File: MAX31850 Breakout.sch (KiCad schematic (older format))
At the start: 11 parts, among them J1 Conn_01x02, J2 Conn_01x03, U1 MAX31850KATB

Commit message: Move library and datasheet folders around
See https://hackaday.com/2017/05/18/kicad-best-practises-library-management/ for more info
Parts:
- U1: symbol MAX31850~Breakout:MAX31850KATB -> MAX31850_Breakout:MAX31850_Breakout_MAX31850KATB
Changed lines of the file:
@@
 $EndDescr
 $Comp
-L MAX31850~Breakout:MAX31850KATB U1
+L MAX31850_Breakout:MAX31850_Breakout_MAX31850KATB U1
 U 1 1 5E73EC25
 P 5300 3300

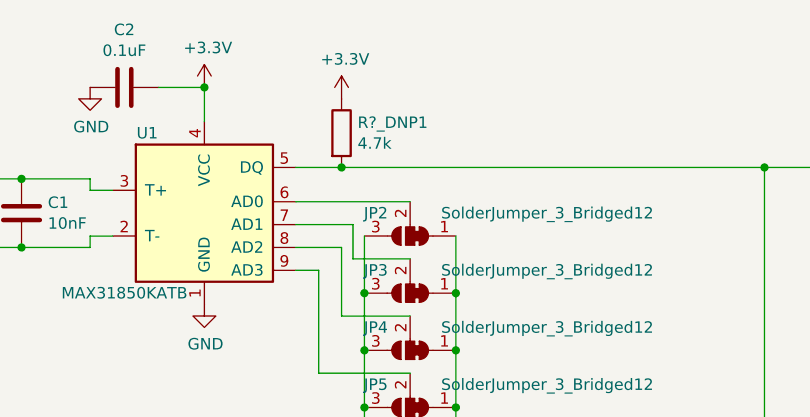
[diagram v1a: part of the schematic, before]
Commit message: Assign footprints
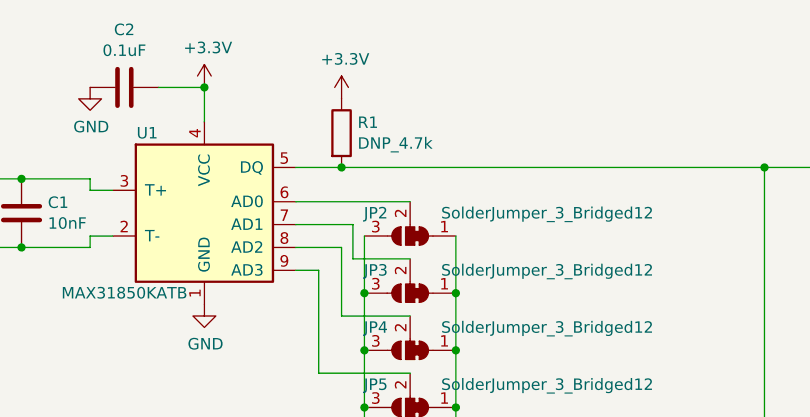
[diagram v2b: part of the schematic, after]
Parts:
- C1, C2: footprint (none) -> 0 - GIE SMD Passive Components:C_0603_1608Metric
- J1: footprint (none) -> 0 - GIE Connectors, Terminal Blocks:TerminalBlock_Phoenix_PT-1,5-2-5.0-H_1x02_P5.00mm_Horizontal
- J2: footprint (none) -> Connector_PinHeader_2.54mm:PinHeader_1x03_P2.54mm_Vertical
- JP1, JP2, JP3, JP4, JP5: footprint (none) -> Jumper:SolderJumper-3_P1.3mm_Bridged12_RoundedPad1.0x1.5mm
- R1: renamed from R?_DNP1; value 4.7k -> DNP_4.7k; footprint (none) -> 0 - GIE SMD Passive Components:R_0603_1608Metric
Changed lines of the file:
@@
 F 0 "JP2" H 6350 3300 50  0000 C CNN
 F 1 "SolderJumper_3_Bridged12" H 5600 3300 50  0000 C CNN
-F 2 "" H 6200 3400 50  0001 C CNN
+F 2 "Jumper:SolderJumper-3_P1.3mm_Bridged12_RoundedPad1.0x1.5mm" H 6200 3400 50  0001 C CNN
 F 3 "~" H 6200 3400 50  0001 C CNN
 	1    6200 3400
@@
 F 0 "JP3" H 6350 3550 50  0000 C CNN
 F 1 "SolderJumper_3_Bridged12" H 5600 3550 50  0000 C CNN
-F 2 "" H 6200 3650 50  0001 C CNN
+F 2 "Jumper:SolderJumper-3_P1.3mm_Bridged12_RoundedPad1.0x1.5mm" H 6200 3650 50  0001 C CNN
 F 3 "~" H 6200 3650 50  0001 C CNN
 	1    6200 3650
@@
 F 0 "JP4" H 6350 3800 50  0000 C CNN
 F 1 "SolderJumper_3_Bridged12" H 5600 3800 50  0000 C CNN
-F 2 "" H 6200 3900 50  0001 C CNN
+F 2 "Jumper:SolderJumper-3_P1.3mm_Bridged12_RoundedPad1.0x1.5mm" H 6200 3900 50  0001 C CNN
 F 3 "~" H 6200 3900 50  0001 C CNN
 	1    6200 3900
@@
 F 0 "JP5" H 6350 4050 50  0000 C CNN
 F 1 "SolderJumper_3_Bridged12" H 5600 4050 50  0000 C CNN
-F 2 "" H 6200 4150 50  0001 C CNN
+F 2 "Jumper:SolderJumper-3_P1.3mm_Bridged12_RoundedPad1.0x1.5mm" H 6200 4150 50  0001 C CNN
 F 3 "~" H 6200 4150 50  0001 C CNN
 	1    6200 4150
@@
 F 0 "JP1" V 6200 4750 50  0000 C CNN
 F 1 "SolderJumper_3_Bridged12" V 6100 5200 50  0000 C CNN
-F 2 "" H 6150 4650 50  0001 C CNN
+F 2 "Jumper:SolderJumper-3_P1.3mm_Bridged12_RoundedPad1.0x1.5mm" H 6150 4650 50  0001 C CNN
 F 3 "~" H 6150 4650 50  0001 C CNN
 	1    6150 4650
@@
 $EndComp
 $Comp
-L Device:R R?_DNP1
-U 1 1 5E7522C3
-P 5900 2950
-F 0 "R?_DNP1" H 5970 2996 50  0000 L CNN
-F 1 "4.7k" H 5970 2905 50  0000 L CNN
-F 2 "" V 5830 2950 50  0001 C CNN
-F 3 "~" H 5900 2950 50  0001 C CNN
-	1    5900 2950
-	1    0    0    -1
-$EndComp
-$Comp
 L Device:C C2
 U 1 1 5E752F56
@@
 F 0 "C2" V 4698 2750 50  0000 C CNN
 F 1 "0.1uF" V 4789 2750 50  0000 C CNN
-F 2 "" H 4988 2600 50  0001 C CNN
+F 2 "0 - GIE SMD Passive Components:C_0603_1608Metric" H 4988 2600 50  0001 C CNN
 F 3 "~" H 4950 2750 50  0001 C CNN
 	1    4950 2750
@@
 F 0 "J2" H 8730 3042 50  0000 L CNN
 F 1 "Conn_01x03" H 8730 2951 50  0000 L CNN
-F 2 "" H 8650 3000 50  0001 C CNN
+F 2 "Connector_PinHeader_2.54mm:PinHeader_1x03_P2.54mm_Vertical" H 8650 3000 50  0001 C CNN
 F 3 "~" H 8650 3000 50  0001 C CNN
 	1    8650 3000
@@
 F 0 "C1" H 4615 3346 50  0000 L CNN
 F 1 "10nF" H 4615 3255 50  0000 L CNN
-F 2 "" H 4538 3150 50  0001 C CNN
+F 2 "0 - GIE SMD Passive Components:C_0603_1608Metric" H 4538 3150 50  0001 C CNN
 F 3 "~" H 4500 3300 50  0001 C CNN
 	1    4500 3300
@@
 F 0 "J1" H 3868 3025 50  0000 C CNN
 F 1 "Conn_01x02" H 3868 3116 50  0000 C CNN
-F 2 "" H 3950 3350 50  0001 C CNN
+F 2 "0 - GIE Connectors, Terminal Blocks:TerminalBlock_Phoenix_PT-1,5-2-5.0-H_1x02_P5.00mm_Horizontal" H 3950 3350 50  0001 C CNN
 F 3 "~" H 3950 3350 50  0001 C CNN
 	1    3950 3350
@@
 Wire Wire Line
 	7750 3100 8450 3100
+$Comp
+L Device:R R1
+U 1 1 5E7522C3
+P 5900 2950
+F 0 "R1" H 5970 2996 50  0000 L CNN
+F 1 "DNP_4.7k" H 5970 2905 50  0000 L CNN
+F 2 "0 - GIE SMD Passive Components:R_0603_1608Metric" V 5830 2950 50  0001 C CNN
+F 3 "~" H 5900 2950 50  0001 C CNN
+	1    5900 2950
+	1    0    0    -1
+$EndComp
 $EndSCHEMATC

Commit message: Update Jumper component, label all nets
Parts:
- JP1, JP2, JP3, JP4, JP5: symbol Jumper:SolderJumper_3_Bridged12 -> 0-GIE_SMD_Jumpers:SolderJumper_3_Bridged12
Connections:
- net T-: now reaches C1.2, J1.1 (Pin_1), U1.2 (T-)
- net T+: now reaches C1.1, J1.2 (Pin_2), U1.3 (T+)
- net DQ: now reaches J2.3 (Pin_3), JP1.3 (B), R1.2, U1.5 (DQ)
- net AD0: now reaches JP2.2 (C), U1.6 (AD0)
- net AD1: now reaches JP3.2 (C), U1.7 (AD1)
- net AD2: now reaches JP4.2 (C), U1.8 (AD2)
- net AD3: now reaches JP5.2 (C), U1.9 (AD3)
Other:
- moved on the sheet: JP1, JP3, JP4, JP5
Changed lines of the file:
@@
 	1    0    0    -1
 $EndComp
-$Comp
-L Jumper:SolderJumper_3_Bridged12 JP2
-U 1 1 5E7420FC
-P 6200 3400
-F 0 "JP2" H 6350 3300 50  0000 C CNN
-F 1 "SolderJumper_3_Bridged12" H 5600 3300 50  0000 C CNN
-F 2 "Jumper:SolderJumper-3_P1.3mm_Bridged12_RoundedPad1.0x1.5mm" H 6200 3400 50  0001 C CNN
-F 3 "~" H 6200 3400 50  0001 C CNN
-	1    6200 3400
-	-1   0    0    1
-$EndComp
-$Comp
-L Jumper:SolderJumper_3_Bridged12 JP3
-U 1 1 5E746EFF
-P 6200 3650
-F 0 "JP3" H 6350 3550 50  0000 C CNN
-F 1 "SolderJumper_3_Bridged12" H 5600 3550 50  0000 C CNN
-F 2 "Jumper:SolderJumper-3_P1.3mm_Bridged12_RoundedPad1.0x1.5mm" H 6200 3650 50  0001 C CNN
-F 3 "~" H 6200 3650 50  0001 C CNN
-	1    6200 3650
-	-1   0    0    1
-$EndComp
-$Comp
-L Jumper:SolderJumper_3_Bridged12 JP4
-U 1 1 5E747464
-P 6200 3900
-F 0 "JP4" H 6350 3800 50  0000 C CNN
-F 1 "SolderJumper_3_Bridged12" H 5600 3800 50  0000 C CNN
-F 2 "Jumper:SolderJumper-3_P1.3mm_Bridged12_RoundedPad1.0x1.5mm" H 6200 3900 50  0001 C CNN
-F 3 "~" H 6200 3900 50  0001 C CNN
-	1    6200 3900
-	-1   0    0    1
-$EndComp
-$Comp
-L Jumper:SolderJumper_3_Bridged12 JP5
-U 1 1 5E7479F9
-P 6200 4150
-F 0 "JP5" H 6350 4050 50  0000 C CNN
-F 1 "SolderJumper_3_Bridged12" H 5600 4050 50  0000 C CNN
-F 2 "Jumper:SolderJumper-3_P1.3mm_Bridged12_RoundedPad1.0x1.5mm" H 6200 4150 50  0001 C CNN
-F 3 "~" H 6200 4150 50  0001 C CNN
-	1    6200 4150
-	-1   0    0    1
-$EndComp
-$Comp
-L power:GND #PWR06
-U 1 1 5E74B9A8
-P 6400 4200
-F 0 "#PWR06" H 6400 3950 50  0001 C CNN
-F 1 "GND" H 6405 4027 50  0000 C CNN
-F 2 "" H 6400 4200 50  0001 C CNN
-F 3 "" H 6400 4200 50  0001 C CNN
-	1    6400 4200
-	1    0    0    -1
-$EndComp
-$Comp
-L Jumper:SolderJumper_3_Bridged12 JP1
-U 1 1 5E74BD6C
-P 6150 4650
-F 0 "JP1" V 6200 4750 50  0000 C CNN
-F 1 "SolderJumper_3_Bridged12" V 6100 5200 50  0000 C CNN
-F 2 "Jumper:SolderJumper-3_P1.3mm_Bridged12_RoundedPad1.0x1.5mm" H 6150 4650 50  0001 C CNN
-F 3 "~" H 6150 4650 50  0001 C CNN
-	1    6150 4650
-	0    1    1    0
-$EndComp
-Wire Wire Line
-	6000 4650 6000 4150
-Connection ~ 6000 3650
-Wire Wire Line
-	6000 3650 6000 3400
-Connection ~ 6000 3900
-Wire Wire Line
-	6000 3900 6000 3650
-Connection ~ 6000 4150
-Wire Wire Line
-	6000 4150 6000 3900
-Wire Wire Line
-	6400 3400 6400 3650
-Connection ~ 6400 3650
-Wire Wire Line
-	6400 3650 6400 3900
-Connection ~ 6400 3900
-Wire Wire Line
-	6400 3900 6400 4150
-Connection ~ 6400 4150
-Wire Wire Line
-	6400 4150 6400 4200
 Wire Wire Line
 	6200 3250 5700 3250
-Wire Wire Line
-	6200 3500 5950 3500
-Wire Wire Line
-	5950 3500 5950 3350
-Wire Wire Line
-	5950 3350 5700 3350
-Wire Wire Line
-	5700 3450 5900 3450
-Wire Wire Line
-	5900 3450 5900 3750
-Wire Wire Line
-	5900 3750 6200 3750
-Wire Wire Line
-	6200 4000 5800 4000
-Wire Wire Line
-	5800 4000 5800 3550
-Wire Wire Line
-	5800 3550 5700 3550
-$Comp
-L power:+3.3V #PWR05
-U 1 1 5E7518A6
-P 6150 4450
-F 0 "#PWR05" H 6150 4300 50  0001 C CNN
-F 1 "+3.3V" H 6165 4623 50  0000 C CNN
-F 2 "" H 6150 4450 50  0001 C CNN
-F 3 "" H 6150 4450 50  0001 C CNN
-	1    6150 4450
-	1    0    0    -1
-$EndComp
 $Comp
 L Device:C C2
@@
 	1    0    0    -1
 $EndComp
-Wire Wire Line
-	5900 3100 7750 3100
-Connection ~ 5900 3100
 $Comp
 L power:+3.3V #PWR04
@@
 L power:GND #PWR07
 U 1 1 5E757CA6
-P 8250 2850
-F 0 "#PWR07" H 8250 2600 50  0001 C CNN
-F 1 "GND" H 8255 2677 50  0000 C CNN
-F 2 "" H 8250 2850 50  0001 C CNN
-F 3 "" H 8250 2850 50  0001 C CNN
-	1    8250 2850
+P 8200 3000
+F 0 "#PWR07" H 8200 2750 50  0001 C CNN
+F 1 "GND" H 8205 2827 50  0000 C CNN
+F 2 "" H 8200 3000 50  0001 C CNN
+F 3 "" H 8200 3000 50  0001 C CNN
+	1    8200 3000
 	1    0    0    -1
 $EndComp
@@
 L power:+3.3V #PWR08
 U 1 1 5E7589FC
-P 8450 2900
-F 0 "#PWR08" H 8450 2750 50  0001 C CNN
-F 1 "+3.3V" H 8465 3073 50  0000 C CNN
-F 2 "" H 8450 2900 50  0001 C CNN
-F 3 "" H 8450 2900 50  0001 C CNN
-	1    8450 2900
-	1    0    0    -1
-$EndComp
-Wire Wire Line
-	8250 2850 8350 2850
-Wire Wire Line
-	8350 2850 8350 3000
-Wire Wire Line
-	8350 3000 8450 3000
+P 8200 2900
+F 0 "#PWR08" H 8200 2750 50  0001 C CNN
+F 1 "+3.3V" H 8215 3073 50  0000 C CNN
+F 2 "" H 8200 2900 50  0001 C CNN
+F 3 "" H 8200 2900 50  0001 C CNN
+	1    8200 2900
+	1    0    0    -1
+$EndComp
 $Comp
 L Device:C C1
@@
 Wire Wire Line
 	4300 3150 4500 3150
-Wire Wire Line
-	7750 3100 7750 4850
-Wire Wire Line
-	7750 4850 6150 4850
-Connection ~ 7750 3100
-Wire Wire Line
-	7750 3100 8450 3100
 $Comp
 L Device:R R1
@@
 	1    0    0    -1
 $EndComp
+$Comp
+L power:PWR_FLAG #FLG0101
+U 1 1 5E76A609
+P 8200 2900
+F 0 "#FLG0101" H 8200 2975 50  0001 C CNN
+F 1 "PWR_FLAG" V 8200 3027 50  0000 L CNN
+F 2 "" H 8200 2900 50  0001 C CNN
+F 3 "~" H 8200 2900 50  0001 C CNN
+	1    8200 2900
+	0    -1   -1   0
+$EndComp
+Text Label 8450 3100 2    50   ~ 0
+DQ
+Text Label 5700 3100 0    50   ~ 0
+DQ
+Text Label 6150 5000 3    50   ~ 0
+DQ
+Wire Wire Line
+	8200 3000 8450 3000
+Connection ~ 8200 2900
+Wire Wire Line
+	8200 2900 8450 2900
+$Comp
+L power:PWR_FLAG #FLG0102
+U 1 1 5E771B67
+P 8200 3000
+F 0 "#FLG0102" H 8200 3075 50  0001 C CNN
+F 1 "PWR_FLAG" V 8200 3127 50  0000 L CNN
+F 2 "" H 8200 3000 50  0001 C CNN
+F 3 "~" H 8200 3000 50  0001 C CNN
+	1    8200 3000
+	0    -1   -1   0
+$EndComp
+Connection ~ 8200 3000
+Text Label 5700 3250 0    50   ~ 0
+AD0
+Text Label 5700 3350 0    50   ~ 0
+AD1
+Text Label 5700 3450 0    50   ~ 0
+AD2
+Text Label 5700 3550 0    50   ~ 0
+AD3
+$Comp
+L power:+3.3V #PWR05
+U 1 1 5E7518A6
+P 6150 4600
+F 0 "#PWR05" H 6150 4450 50  0001 C CNN
+F 1 "+3.3V" H 6165 4773 50  0000 C CNN
+F 2 "" H 6150 4600 50  0001 C CNN
+F 3 "" H 6150 4600 50  0001 C CNN
+	1    6150 4600
+	1    0    0    -1
+$EndComp
+Wire Wire Line
+	6400 4300 6400 4350
+Wire Wire Line
+	6000 4800 6000 4300
+$Comp
+L power:GND #PWR06
+U 1 1 5E74B9A8
+P 6400 4350
+F 0 "#PWR06" H 6400 4100 50  0001 C CNN
+F 1 "GND" H 6405 4177 50  0000 C CNN
+F 2 "" H 6400 4350 50  0001 C CNN
+F 3 "" H 6400 4350 50  0001 C CNN
+	1    6400 4350
+	1    0    0    -1
+$EndComp
+$Comp
+L 0-GIE_SMD_Jumpers:SolderJumper_3_Bridged12 JP5
+U 1 1 5E7479F9
+P 6200 4300
+F 0 "JP5" H 6350 4200 50  0000 C CNN
+F 1 "SolderJumper_3_Bridged12" H 5600 4200 50  0000 C CNN
+F 2 "Jumper:SolderJumper-3_P1.3mm_Bridged12_RoundedPad1.0x1.5mm" H 6200 4300 50  0001 C CNN
+F 3 "~" H 6200 4300 50  0001 C CNN
+	1    6200 4300
+	-1   0    0    1
+$EndComp
+$Comp
+L 0-GIE_SMD_Jumpers:SolderJumper_3_Bridged12 JP4
+U 1 1 5E747464
+P 6200 4000
+F 0 "JP4" H 6350 3900 50  0000 C CNN
+F 1 "SolderJumper_3_Bridged12" H 5600 3900 50  0000 C CNN
+F 2 "Jumper:SolderJumper-3_P1.3mm_Bridged12_RoundedPad1.0x1.5mm" H 6200 4000 50  0001 C CNN
+F 3 "~" H 6200 4000 50  0001 C CNN
+	1    6200 4000
+	-1   0    0    1
+$EndComp
+$Comp
+L 0-GIE_SMD_Jumpers:SolderJumper_3_Bridged12 JP3
+U 1 1 5E746EFF
+P 6200 3700
+F 0 "JP3" H 6350 3600 50  0000 C CNN
+F 1 "SolderJumper_3_Bridged12" H 5600 3600 50  0000 C CNN
+F 2 "Jumper:SolderJumper-3_P1.3mm_Bridged12_RoundedPad1.0x1.5mm" H 6200 3700 50  0001 C CNN
+F 3 "~" H 6200 3700 50  0001 C CNN
+	1    6200 3700
+	-1   0    0    1
+$EndComp
+$Comp
+L 0-GIE_SMD_Jumpers:SolderJumper_3_Bridged12 JP2
+U 1 1 5E7420FC
+P 6200 3400
+F 0 "JP2" H 6350 3300 50  0000 C CNN
+F 1 "SolderJumper_3_Bridged12" H 5600 3300 50  0000 C CNN
+F 2 "Jumper:SolderJumper-3_P1.3mm_Bridged12_RoundedPad1.0x1.5mm" H 6200 3400 50  0001 C CNN
+F 3 "~" H 6200 3400 50  0001 C CNN
+	1    6200 3400
+	-1   0    0    1
+$EndComp
+Text Label 6200 3550 0    50   ~ 0
+AD1
+Text Label 6200 3850 0    50   ~ 0
+AD2
+Text Label 6200 4150 0    50   ~ 0
+AD3
+Wire Wire Line
+	6000 3400 6000 3700
+Connection ~ 6000 4300
+Connection ~ 6000 3700
+Wire Wire Line
+	6000 3700 6000 4000
+Connection ~ 6000 4000
+Wire Wire Line
+	6000 4000 6000 4300
+Wire Wire Line
+	6400 3400 6400 3700
+Connection ~ 6400 4300
+Connection ~ 6400 3700
+Wire Wire Line
+	6400 3700 6400 4000
+Connection ~ 6400 4000
+Wire Wire Line
+	6400 4000 6400 4300
+$Comp
+L 0-GIE_SMD_Jumpers:SolderJumper_3_Bridged12 JP1
+U 1 1 5E74BD6C
+P 6150 4800
+F 0 "JP1" V 6200 4900 50  0000 C CNN
+F 1 "SolderJumper_3_Bridged12" V 6100 5350 50  0000 C CNN
+F 2 "Jumper:SolderJumper-3_P1.3mm_Bridged12_RoundedPad1.0x1.5mm" H 6150 4800 50  0001 C CNN
+F 3 "~" H 6150 4800 50  0001 C CNN
+	1    6150 4800
+	0    1    1    0
+$EndComp
+Text Label 4700 3150 0    50   ~ 0
+T+
+Text Label 4700 3450 0    50   ~ 0
+T-
 $EndSCHEMATC

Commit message: Update project library
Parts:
- U1: symbol MAX31850_Breakout:MAX31850_Breakout_MAX31850KATB -> MAX31850_Breakout:MAX31850KATB
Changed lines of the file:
@@
 $EndDescr
 $Comp
-L MAX31850_Breakout:MAX31850_Breakout_MAX31850KATB U1
+L MAX31850_Breakout:MAX31850KATB U1
 U 1 1 5E73EC25
 P 5300 3300

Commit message: Layout and Route PCB
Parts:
- renumbered JP2 to AD0, JP3 to AD1, JP4 to AD2, JP5 to AD3, JP1 to AD_SRC1
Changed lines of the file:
@@
 $EndComp
 $Comp
-L 0-GIE_SMD_Jumpers:SolderJumper_3_Bridged12 JP5
+L 0-GIE_SMD_Jumpers:SolderJumper_3_Bridged12 AD3
 U 1 1 5E7479F9
 P 6200 4300
-F 0 "JP5" H 6350 4200 50  0000 C CNN
+F 0 "AD3" H 6350 4200 50  0000 C CNN
 F 1 "SolderJumper_3_Bridged12" H 5600 4200 50  0000 C CNN
 F 2 "Jumper:SolderJumper-3_P1.3mm_Bridged12_RoundedPad1.0x1.5mm" H 6200 4300 50  0001 C CNN
@@
 $EndComp
 $Comp
-L 0-GIE_SMD_Jumpers:SolderJumper_3_Bridged12 JP4
+L 0-GIE_SMD_Jumpers:SolderJumper_3_Bridged12 AD2
 U 1 1 5E747464
 P 6200 4000
-F 0 "JP4" H 6350 3900 50  0000 C CNN
+F 0 "AD2" H 6350 3900 50  0000 C CNN
 F 1 "SolderJumper_3_Bridged12" H 5600 3900 50  0000 C CNN
 F 2 "Jumper:SolderJumper-3_P1.3mm_Bridged12_RoundedPad1.0x1.5mm" H 6200 4000 50  0001 C CNN
@@
 $EndComp
 $Comp
-L 0-GIE_SMD_Jumpers:SolderJumper_3_Bridged12 JP3
+L 0-GIE_SMD_Jumpers:SolderJumper_3_Bridged12 AD1
 U 1 1 5E746EFF
 P 6200 3700
-F 0 "JP3" H 6350 3600 50  0000 C CNN
+F 0 "AD1" H 6350 3600 50  0000 C CNN
 F 1 "SolderJumper_3_Bridged12" H 5600 3600 50  0000 C CNN
 F 2 "Jumper:SolderJumper-3_P1.3mm_Bridged12_RoundedPad1.0x1.5mm" H 6200 3700 50  0001 C CNN
@@
 $EndComp
 $Comp
-L 0-GIE_SMD_Jumpers:SolderJumper_3_Bridged12 JP2
+L 0-GIE_SMD_Jumpers:SolderJumper_3_Bridged12 AD0
 U 1 1 5E7420FC
 P 6200 3400
-F 0 "JP2" H 6350 3300 50  0000 C CNN
+F 0 "AD0" H 6350 3300 50  0000 C CNN
 F 1 "SolderJumper_3_Bridged12" H 5600 3300 50  0000 C CNN
 F 2 "Jumper:SolderJumper-3_P1.3mm_Bridged12_RoundedPad1.0x1.5mm" H 6200 3400 50  0001 C CNN
@@
 	6400 4000 6400 4300
 $Comp
-L 0-GIE_SMD_Jumpers:SolderJumper_3_Bridged12 JP1
+L 0-GIE_SMD_Jumpers:SolderJumper_3_Bridged12 AD_SRC1
 U 1 1 5E74BD6C
 P 6150 4800
-F 0 "JP1" V 6200 4900 50  0000 C CNN
+F 0 "AD_SRC1" V 6200 5000 50  0000 C CNN
 F 1 "SolderJumper_3_Bridged12" V 6100 5350 50  0000 C CNN
 F 2 "Jumper:SolderJumper-3_P1.3mm_Bridged12_RoundedPad1.0x1.5mm" H 6150 4800 50  0001 C CNN

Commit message: Replace footprints with local copy
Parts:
- AD0, AD1, AD2, AD3, AD_SRC1: footprint Jumper:SolderJumper-3_P1.3mm_Bridged12_RoundedPad1.0x1.5mm -> MAX31850-Breakout-footprints:SolderJumper-3_P1.3mm_Bridged12_RoundedPad1.0x1.5mm
- C1, C2: footprint 0 - GIE SMD Passive Components:C_0603_1608Metric -> MAX31850-Breakout-footprints:C_0603_1608Metric
- J1: footprint 0 - GIE Connectors, Terminal Blocks:TerminalBlock_Phoenix_PT-1,5-2-5.0-H_1x02_P5.00mm_Horizontal -> MAX31850-Breakout-footprints:TerminalBlock_Phoenix_PT-1,5-2-5.0-H_1x02_P5.00mm_Horizontal
- J2: footprint Connector_PinHeader_2.54mm:PinHeader_1x03_P2.54mm_Vertical -> MAX31850-Breakout-footprints:PinHeader_1x03_P2.54mm_Vertical
- R1: footprint 0 - GIE SMD Passive Components:R_0603_1608Metric -> MAX31850-Breakout-footprints:R_0603_1608Metric
- U1: footprint MAX31850-Breakout:TDFN-10-1EP_3x4mm_P0.5mm_EP1.75x2.7mm -> MAX31850-Breakout-footprints:TDFN-10-1EP_3x4mm_P0.5mm_EP1.75x2.7mm
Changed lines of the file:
@@
 EESchema Schematic File Version 4
+LIBS:MAX31850 Breakout-cache
 EELAYER 30 0
 EELAYER END
@@
 F 0 "U1" H 5050 3650 50  0000 C CNN
 F 1 "MAX31850KATB" H 4950 2950 50  0000 C CNN
-F 2 "MAX31850-Breakout:TDFN-10-1EP_3x4mm_P0.5mm_EP1.75x2.7mm" H 6300 2950 50  0001 C CIN
+F 2 "MAX31850-Breakout-footprints:TDFN-10-1EP_3x4mm_P0.5mm_EP1.75x2.7mm" H 6300 2950 50  0001 C CIN
 F 3 "https://datasheets.maximintegrated.com/en/ds/MAX31850-MAX31851.pdf" H 5300 3300 50  0001 C CNN
 	1    5300 3300
@@
 F 0 "C2" V 4698 2750 50  0000 C CNN
 F 1 "0.1uF" V 4789 2750 50  0000 C CNN
-F 2 "0 - GIE SMD Passive Components:C_0603_1608Metric" H 4988 2600 50  0001 C CNN
+F 2 "MAX31850-Breakout-footprints:C_0603_1608Metric" H 4988 2600 50  0001 C CNN
 F 3 "~" H 4950 2750 50  0001 C CNN
 	1    4950 2750
@@
 F 0 "J2" H 8730 3042 50  0000 L CNN
 F 1 "Conn_01x03" H 8730 2951 50  0000 L CNN
-F 2 "Connector_PinHeader_2.54mm:PinHeader_1x03_P2.54mm_Vertical" H 8650 3000 50  0001 C CNN
+F 2 "MAX31850-Breakout-footprints:PinHeader_1x03_P2.54mm_Vertical" H 8650 3000 50  0001 C CNN
 F 3 "~" H 8650 3000 50  0001 C CNN
 	1    8650 3000
@@
 F 0 "C1" H 4615 3346 50  0000 L CNN
 F 1 "10nF" H 4615 3255 50  0000 L CNN
-F 2 "0 - GIE SMD Passive Components:C_0603_1608Metric" H 4538 3150 50  0001 C CNN
+F 2 "MAX31850-Breakout-footprints:C_0603_1608Metric" H 4538 3150 50  0001 C CNN
 F 3 "~" H 4500 3300 50  0001 C CNN
 	1    4500 3300
@@
 F 0 "J1" H 3868 3025 50  0000 C CNN
 F 1 "Conn_01x02" H 3868 3116 50  0000 C CNN
-F 2 "0 - GIE Connectors, Terminal Blocks:TerminalBlock_Phoenix_PT-1,5-2-5.0-H_1x02_P5.00mm_Horizontal" H 3950 3350 50  0001 C CNN
+F 2 "MAX31850-Breakout-footprints:TerminalBlock_Phoenix_PT-1,5-2-5.0-H_1x02_P5.00mm_Horizontal" H 3950 3350 50  0001 C CNN
 F 3 "~" H 3950 3350 50  0001 C CNN
 	1    3950 3350
@@
 F 0 "R1" H 5970 2996 50  0000 L CNN
 F 1 "DNP_4.7k" H 5970 2905 50  0000 L CNN
-F 2 "0 - GIE SMD Passive Components:R_0603_1608Metric" V 5830 2950 50  0001 C CNN
+F 2 "MAX31850-Breakout-footprints:R_0603_1608Metric" V 5830 2950 50  0001 C CNN
 F 3 "~" H 5900 2950 50  0001 C CNN
 	1    5900 2950
@@
 F 0 "AD3" H 6350 4200 50  0000 C CNN
 F 1 "SolderJumper_3_Bridged12" H 5600 4200 50  0000 C CNN
-F 2 "Jumper:SolderJumper-3_P1.3mm_Bridged12_RoundedPad1.0x1.5mm" H 6200 4300 50  0001 C CNN
+F 2 "MAX31850-Breakout-footprints:SolderJumper-3_P1.3mm_Bridged12_RoundedPad1.0x1.5mm" H 6200 4300 50  0001 C CNN
 F 3 "~" H 6200 4300 50  0001 C CNN
 	1    6200 4300
@@
 F 0 "AD2" H 6350 3900 50  0000 C CNN
 F 1 "SolderJumper_3_Bridged12" H 5600 3900 50  0000 C CNN
-F 2 "Jumper:SolderJumper-3_P1.3mm_Bridged12_RoundedPad1.0x1.5mm" H 6200 4000 50  0001 C CNN
+F 2 "MAX31850-Breakout-footprints:SolderJumper-3_P1.3mm_Bridged12_RoundedPad1.0x1.5mm" H 6200 4000 50  0001 C CNN
 F 3 "~" H 6200 4000 50  0001 C CNN
 	1    6200 4000
@@
 F 0 "AD1" H 6350 3600 50  0000 C CNN
 F 1 "SolderJumper_3_Bridged12" H 5600 3600 50  0000 C CNN
-F 2 "Jumper:SolderJumper-3_P1.3mm_Bridged12_RoundedPad1.0x1.5mm" H 6200 3700 50  0001 C CNN
+F 2 "MAX31850-Breakout-footprints:SolderJumper-3_P1.3mm_Bridged12_RoundedPad1.0x1.5mm" H 6200 3700 50  0001 C CNN
 F 3 "~" H 6200 3700 50  0001 C CNN
 	1    6200 3700
@@
 F 0 "AD0" H 6350 3300 50  0000 C CNN
 F 1 "SolderJumper_3_Bridged12" H 5600 3300 50  0000 C CNN
-F 2 "Jumper:SolderJumper-3_P1.3mm_Bridged12_RoundedPad1.0x1.5mm" H 6200 3400 50  0001 C CNN
+F 2 "MAX31850-Breakout-footprints:SolderJumper-3_P1.3mm_Bridged12_RoundedPad1.0x1.5mm" H 6200 3400 50  0001 C CNN
 F 3 "~" H 6200 3400 50  0001 C CNN
 	1    6200 3400
@@
 F 0 "AD_SRC1" V 6200 5000 50  0000 C CNN
 F 1 "SolderJumper_3_Bridged12" V 6100 5350 50  0000 C CNN
-F 2 "Jumper:SolderJumper-3_P1.3mm_Bridged12_RoundedPad1.0x1.5mm" H 6150 4800 50  0001 C CNN
+F 2 "MAX31850-Breakout-footprints:SolderJumper-3_P1.3mm_Bridged12_RoundedPad1.0x1.5mm" H 6150 4800 50  0001 C CNN
 F 3 "~" H 6150 4800 50  0001 C CNN
 	1    6150 4800
